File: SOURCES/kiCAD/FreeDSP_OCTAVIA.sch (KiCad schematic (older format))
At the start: 147 parts, among them IC1 TPS5430DDA, J13 Conn_01x05, J2 DC12V-IN, J4 Header_01x06, J8 Header_01x04, P1 Conn_02x20_Odd_Even, Q1 AO3401A, Q14 2N7002, Q2 MMBT5401, Q3 2N7002, Q4 MMBT5401, Q5 AO3401A, Q6 2N7002, Q7 AO3401A, Q8 2N7002, Q9 2N7002, SW1 SW_Push, SW2 SW_SPDT, SW3 SW_SPDT, U1 GP1UXC41QS, U3 AMS1117-5.0, U5 TPS5430DDA, U6 LMC555CMX, U7 AMS1117-3.3, U8 LM2611AMFX

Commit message: Updated version0.2
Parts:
- A1, P1: JLPCB# NOP -> HAND
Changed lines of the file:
@@
 F 2 "Connector_PinSocket_2.54mm:PinSocket_2x20_P2.54mm_Vertical" H 900 6900 50  0001 C CNN
 F 3 "" H 900 6900 50  0001 C CNN
-F 4 "NOP" H 5750 7850 50  0001 C CNN "JLPCB#"
+F 4 "HAND" H 5750 7850 50  0001 C CNN "JLPCB#"
 	1    5750 7850
 	1    0    0    -1
@@
 F 2 "MyLibrary:Combo384" H 8975 8075 50  0001 C CNN
 F 3 "" H 8975 8075 50  0001 C CNN
-F 4 "NOP" H 9175 8125 50  0001 C CNN "JLPCB#"
+F 4 "HAND" H 9175 8125 50  0001 C CNN "JLPCB#"
 	1    9175 8125
 	1    0    0    -1

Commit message: Version0.2 Board. Reviced PCB design.
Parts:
- added D22, D23: 1N4148W, Diode_SMD:D_SOD-123, symbol MW-ADAU1466BB-rescue:D-CS5368TDM-rescue-RasPiAudioHat-rescue
- added J7: Header_01x04, Connector_PinHeader_2.54mm:PinHeader_1x04_P2.54mm_Vertical, symbol Connector_Generic:Conn_01x04
- added Q32: 2N7002, Package_TO_SOT_SMD:SOT-23_Handsoldering, symbol Transistor_FET:2N7002
- added R49: 3.3k, Resistor_SMD:R_0603_1608Metric, symbol Device:R
- added R50: 10k, Resistor_SMD:R_0805_2012Metric_Pad1.20x1.40mm_HandSolder, symbol MW-ADAU1466BB-rescue:R-CS5368TDM-rescue-RasPiAudioHat-rescue
- added R51: 100k, Resistor_SMD:R_0805_2012Metric_Pad1.20x1.40mm_HandSolder, symbol MW-ADAU1466BB-rescue:R-CS5368TDM-rescue-RasPiAudioHat-rescue
- added TP1: TestPoint_GNDA, TestPoint:TestPoint_THTPad_2.0x2.0mm_Drill1.0mm, symbol Connector:TestPoint_Alt
- added TP2: TestPoint_GND, TestPoint:TestPoint_THTPad_2.0x2.0mm_Drill1.0mm, symbol Connector:TestPoint_Alt
- C12: Description (none) -> for the Power-OFF muting power keep
- C13: footprint Capacitor_THT:CP_Radial_D5.0mm_P2.00mm -> Capacitor_THT:CP_Radial_D10.0mm_P2.50mm_P5.00mm; Description (none) -> for Analog +5V decoupling, Solid-Cap recommended
- C15: Description (none) -> for Negative SMPS Power Integration
- C22: Description (none) -> for the Raspberry-pi Shutdown-Time constant
- C43: Description (none) -> for Raspberry-pi SMPS Power Integration
- C8: Description (none) -> for the Power-ON delay timing
- D19: Description (none) -> Just for check the PC status
- D3: Description (none) -> Remove this if you use extension header
- J13: Description (none) -> for the Optional Source Position LED Indicator
- J2: Description (none) -> for 2.1mm wall Power Supply (DC6.5V to 12V)
- J4: Description (none) -> Optional Serial Cable Header for Raspberry-pi
- J8: Description (none) -> Optional I2C OLED Display Connection for Raspberry-pi
- JP3: Description (none) -> Short this if you use sotware DSP-RESET control
- P1: Description (none) -> for Rapberry-pi
- R100, R101, R102, R103: value 330R -> 1k; JLPCB# C17630 -> C17513
- R33, R7: value 1k -> 3.3k; JLPCB# C17513 -> C22978
- SW1: footprint OPL_Switch:SW2-5.0-6.0X3.0X4.3MM -> Button_Switch_THT:SW_Tactile_SPST_Angled_PTS645Vx83-2LFS
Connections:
- net +3.3VP: now also J8.2 (Pin_2); no longer J8.4 (Pin_4)
- net +3V3: now also J13.1 (Pin_1), R108.1, R49.2
- net +5V: no longer J13.1 (Pin_1)
- net AUX5: no longer Q14.3 (D)
- net GND: now also J7.4 (Pin_4), Q32.2 (S), R51.2, TP2.1; no longer R108.1
- net GNDA: now also TP1.1
- net MUTE: now also D22.2 (A); no longer Q9.1 (G)
- net RP_SDA: now also J8.4 (Pin_4); no longer J8.2 (Pin_2)
- net at D3.1 (A), R6.2: now also J7.2 (Pin_2)
- net at D3.3 (GK), Q8.3 (D): now also J7.3 (Pin_3)
- net ~SEL_USB: now reaches J13.2 (Pin_2), R100.2
- net ~SEL_USB: now also R108.2, Q32.1 (G)
- net at A1.11 (~MUTE): now also Q14.1 (G); no longer D13.2 (A)
- net at D3.4 (RK), Q3.3 (D): now also J7.1 (Pin_1)
- net USB_MUTE: no longer names the net of D12.1 (K), D13.1 (K)
- net USB_MUTE: now also R50.1; no longer Q14.1 (G), R108.2
- new net: D22.1 (K), D23.1 (K), Q9.1 (G), R51.1
- new net: D13.2 (A), Q14.3 (D), R49.1
- new net: D23.2 (A), Q32.3 (D), R50.2
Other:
- note added: "1.6V min."
- note added: "ANODE\nRaspberry-Pi\nUSB\nS/PDIF\nANALOG"
- note added: "BLUE\nGREEN\nANODE\nRED"
- note added: "SDA\nSCL\nVCC\nGND"
- note added: "SOURCE MIN MAX\n\n4:Analog 12 - 15\n3:S/PDIF 9 - 11 \n2:USB 6 - 8\n1:RAS-Pi 3 - 5\n0:MUTE 0 - 2"
- note removed: "1.09V/4.8V"
- note removed: "ANODE\nANALOG\nS/PDIF\nUSB\nRaspberry-Pi"
- note removed: "SOURCE MIN MAX\n\nRAS-Pi 12 - 15\nAmanero 9 - 11 \nS/PDIF 6 - 8\nAnalog 3 - 5\nMUTE 0 - 2"
- moved on the sheet: D12, D13, D19, D3, J13, J8, Q14, Q9, R100, R101, R102, R103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

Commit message: Fixed wrong L/R Connection of RCA Jack
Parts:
- A1: symbol MW-ADAU1466BB-rescue:Combo384-Combo384 -> Combo384:Combo384
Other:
- note added: "(ADC/DAC/Line-Driver Power)"
- note added: "DC9V WALL\nADAPTOR"
- note added: "Muting = +12V\nUnMuting = -4.5V"
- note added: "Power-ON Delay \nTiming CR (5 Sec)"
- note removed: "(ADC/DAC Power)"
- note removed: "DC12V WALL\nADOPTOR"
- note removed: "Power-ON Delay \nTiming CR (.1 Sec)"
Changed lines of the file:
@@
 Sheet 1 3
 Title "FreeDSP OVTAVIA Main Board"
-Date "2023-05-13"
+Date "2023-05-21"
 Rev "0.25"
 Comp ""
@@
 Power-OFF Delay \nTiming CR (40 Sec)
 Text Notes 4650 6100 0    50   ~ 0
-Power-ON Delay \nTiming CR (.1 Sec)
+Power-ON Delay \nTiming CR (5 Sec)
 Wire Notes Line
 	5775 5475 5300 5975
@@
 (DSP Power)
 Text Notes 11800 3225 0    50   ~ 0
-(ADC/DAC Power)
+(ADC/DAC/Line-Driver Power)
 $Comp
 L Device:D_ALT D?
@@
 Connection ~ 5750 4175
 Text Notes 11800 3975 0    50   ~ 0
-(ADC/DAC Power)
+(ADC/DAC/Line-Driver Power)
 $Comp
 L Device:C_Small C?
@@
 Connection ~ 3275 1250
 Text Notes 900  1525 0    79   ~ 16
-DC12V WALL\nADOPTOR
+DC9V WALL\nADAPTOR
 Wire Wire Line
 	3275 1150 3275 1250
@@
 $EndComp
 $Comp
-L MW-ADAU1466BB-rescue:Combo384-Combo384 A1
+L Combo384:Combo384 A1
 U 1 1 6517C675
 P 9175 8125
@@
 Text Notes 1850 7400 0    63   ~ 0
 SDA\nSCL\nVCC\nGND
+Text Notes 7100 2350 0    50   ~ 0
+Muting   = +12V\nUnMuting = -4.5V
 $EndSCHEMATC

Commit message: New Output Driver with Enhanced 4 Layer PCB
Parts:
- added C164: 220uF/6.3V, Capacitor_THT:CP_Radial_D10.0mm_P2.50mm_P5.00mm, symbol Device:CP1_Small
- added R54: 100k, Resistor_SMD:R_0805_2012Metric_Pad1.20x1.40mm_HandSolder, symbol MW-ADAU1466BB-rescue:R-CS5368TDM-rescue-RasPiAudioHat-rescue
- J2: value DC12V-IN -> DC7.5V-9V IN
- R33, R7: JLPCB# C22978 -> C26010
- R71: value 330R -> 3.3k; JLPCB# C17630 -> C26010
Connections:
- net +12V: no longer C37.1, C38.1, L4.2, U8.5 (VIN)
- net +3V3: now also R54.1; no longer Q6.1 (G), R35.1, U8.4 (~SHDN)
- net +5VA: now also U8.4 (~SHDN)
- net -5VA: now also C164.2
- net GNDA: now also C164.1
- net ALWAYS_ON: now reaches C14.1, C18.2, C20.1, C21.1, C5.1, C6.1, C9.2, D10.2 (A), D8.1 (K), IC1.7 (VIN), Q1.2 (S), Q5.2 (S), Q7.3, R15.1, R21.1, R36.1, R5.1, SW2.1 (A), U5.7 (VIN), U6.4 (R), U6.8 (VCC)
- net ALWAYS_ON: now also C37.1, C38.1, L4.2, U8.5 (VIN)
- new net: Q6.1 (G), R35.1, R54.2
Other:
- note added: "Muting = +7.5V\nUnMuting = -4.5V"
- note removed: "Muting = +12V\nUnMuting = -4.5V"
- moved on the sheet: C11, C13, C14, C40, C42, C44, C7, FB2, Q5, Q6, R35, R36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

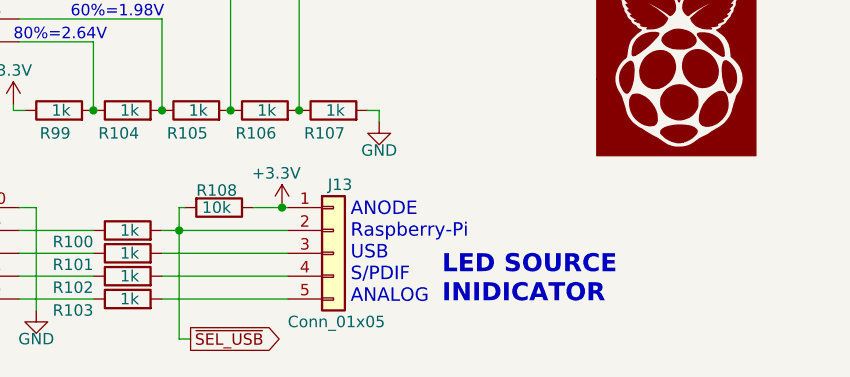
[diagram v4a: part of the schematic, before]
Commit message: Fixed USB Position of Source Selector Switch
Version 0.30 (CCW) USB - RPi - DIG -ANA (CW)
Version 0.31 (CCW) RPi - USB - DIG -ANA (CW)
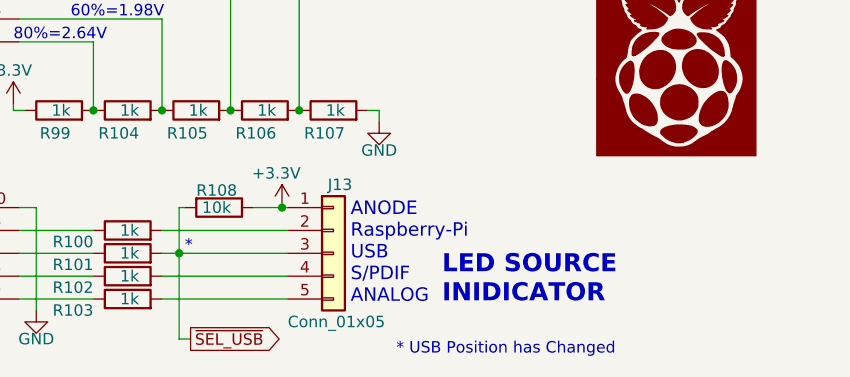
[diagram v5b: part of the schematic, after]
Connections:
- net ~SEL_USB: now also J13.3 (Pin_3), R101.2; no longer J13.2 (Pin_2), R100.2
- new net: J13.2 (Pin_2), R100.2
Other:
- note added: "*"
- note added: "* USB Position has Changed"
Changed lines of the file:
@@
 Sheet 1 3
 Title "FreeDSP OVTAVIA Main Board"
-Date "2023-07-22"
-Rev "0.3"
+Date "2023-07-25"
+Rev "0.31"
 Comp ""
 Comment1 ""
@@
 	4200 10500 4175 10500
 Wire Wire Line
-	4200 10600 3725 10600
-Wire Wire Line
-	3650 10700 4200 10700
+	3650 10700 3725 10700
 Wire Wire Line
 	4200 10800 3650 10800
@@
 Wire Wire Line
 	3750 10500 3725 10500
-Wire Wire Line
-	3725 10500 3725 10600
-Connection ~ 3725 10600
-Wire Wire Line
-	3725 10600 3650 10600
 Text GLabel 3775 11075 2    50   Output ~ 0
 ~SEL_USB
 Wire Wire Line
 	3725 11075 3775 11075
-Wire Wire Line
-	3725 10600 3725 11075
 Text GLabel 9975 9375 0    50   Input ~ 0
 ~SEL_USB
@@
 	15625 2475 15325 2475
 Connection ~ 15325 2475
+Wire Wire Line
+	3650 10600 4200 10600
+Wire Wire Line
+	3725 10500 3725 10700
+Connection ~ 3725 10700
+Wire Wire Line
+	3725 10700 4200 10700
+Wire Wire Line
+	3725 11075 3725 10700
+Text Notes 4675 11150 0    50   ~ 0
+* USB Position has Changed
+Text Notes 3750 10700 0    50   ~ 0
+*
 $EndSCHEMATC

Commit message: Voltage Regulator Changed to LM317
PCB layout is also updated in some of the places.
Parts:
- added R56: 100R, Resistor_SMD:R_0603_1608Metric, symbol Device:R
- added R57: 120R, Resistor_SMD:R_0603_1608Metric, symbol Device:R
- added R58: 330R, Resistor_SMD:R_0603_1608Metric, symbol Device:R
- added R59: 200R, Resistor_SMD:R_0603_1608Metric, symbol Device:R
- added R60: 10R, Resistor_SMD:R_0603_1608Metric, symbol Device:R
- A1: Description (none) -> Amanero or Compatible USB to I2S I/F Board Slot
- D19: Description Just for check the PC status -> Just for check the PC VBUS status
- D3: Description Remove this if you use extension header -> Remove this if you use the Power Status LED extension header
- FL1: Description (none) -> Common mode choke for mains
- IC1, U5: Description (none) -> SMPS for digital part
- J2: Description for 2.1mm wall Power Supply (DC6.5V to 12V) -> for 2.1mm wall Power Supply (DC6.5V to 9V)
- J4: Description Optional Serial Cable Header for Raspberry-pi -> Optional TTL-232R-3V3 Serial Cable Header for Raspberry-pi
- L2, L3, L4, L5: Description (none) -> Metal-Alloy Power Inductor
- MH1: Description (none) -> Mount-hole for Chassis GND
- SW1: Description (none) -> RPI Shutdown/Reboot switch
- SW2: Description (none) -> Mains Power Switch C&K 200MSP1T2B2M7RE, T105MH9AVBE
- SW3: Description (none) -> RPI Power Sub-Switch C&K 200MSP1T2B2M7RE, T105MH9AVBE
- TP1: Description (none) -> TP for Analog Measurement
- TP2: Description (none) -> for Chassis GND Connection
- U1: Description SENSOR REMOTE REC 38.0KHZ 45M -> Optional: Vishay TSOP38238 IR REMOTE SENSOR REC 38.0KHZ 45M
- U3: value AMS1117-5.0 -> LM317AG-TN3-R; footprint Package_TO_SOT_SMD:SOT-223-3_TabPin2 -> Package_TO_SOT_SMD:TO-252-2; symbol Regulator_Linear:AZ1117-ADJ -> Regulator_Linear:LM317_TO-252; Description (none) -> Voltage Regurator for Analog; JLPCB# C6187 -> C75510
- U6: Description (none) -> Timing Controller for RPI PSU
- U7: value AMS1117-3.3 -> LM317AG-TN3-R; footprint Package_TO_SOT_SMD:SOT-223-3_TabPin2 -> Package_TO_SOT_SMD:TO-252-2; symbol Regulator_Linear:AZ1117-ADJ -> Regulator_Linear:LM317_TO-252; Description (none) -> Voltage Regurator for Analog; JLPCB# C6186 -> C75510
- U8: Description (none) -> Negativer 3MHz SMPS
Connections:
- net +3.3VA: now also R57.1
- net +5VA: now also R60.1
- net GND: no longer C140.1
- net GNDA: now also C140.1, R58.1, R59.1; no longer U3.1 (ADJ), U7.1 (ADJ)
- new net: R56.2, R58.2, U3.1 (ADJ)
- new net: R57.2, R59.2, U7.1 (ADJ)
- new net: R56.1, R60.2
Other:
- note added: "1.4MHz Invert SMPS"
- note added: "2.08V"
- note added: "3.75V"
- note added: "C&K 200MSP1T2B2M7RE, T105MH9AVBE"
- note added: "C&K PTS645VL39-2 LFS"
- note added: "RAS-Pi\nSHUT/REBOOT\nSWITCH"
- note removed: "RAS-Pi\nRES/SHUT\nSWITCH"
- moved on the sheet: C40, C42, C44, U7

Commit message: Released for everyone, ready to build.
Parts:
- removed Q14: 2N7002, Package_TO_SOT_SMD:SOT-23_Handsoldering, symbol Transistor_FET:2N7002
- added R61: 0R, Resistor_SMD:R_0603_1608Metric, symbol Device:R
- A1: value Combo384 -> Combo384-Combo384
- C22: Description for the Raspberry-pi Shutdown-Time constant -> Time-Constant Cap for RPI delay-Shutdown
- C23: Description (none) -> Time-Constant Cap for RPI delay-ON
- D1, D11, D12, D13, D2, D22, D23, D4, D5, D6, D7, D8: Description (none) -> Si Switching Diode
- D10, D9: Description (none) -> SBD for charging C32
- D14, D16: Description (none) -> SBD 40V 550mV@5A
- FB13: Description FERRITE BEAD 600 OHM 0603 1LN -> Bead for Analog -VEE rail
- MH2, MH3, MH4, MH5, MH6, MH7: Description (none) -> Mount hole
- MK1, MK2: Description (none) -> Mount hole for Rspberry-pi
- P1: Description for Rapberry-pi -> for Rapberry-pi Slot
- Q2, Q4: Description (none) -> PNP Transistor for anti-pop muting
- Q3, Q32, Q6, Q8, Q9: Description (none) -> N-CHANNEL ENHANCEMENT MODE MOSFET
- R10, R9: Description (none) -> Selectable Exclusive Mount Jumper R
- R40: Description (none) -> Selectable Exclusive Mount Jumper for RESET by RPI feature
- R49: value 3.3k -> 10k; JLPCB# C22978 -> C25804
- R57: value 120R -> 180R
- R59: value 200R -> 270R
- TP1: Description TP for Analog Measurement -> TP for Analog Measurement and Chassis GND Connection
- TP2: Description for Chassis GND Connection -> TP for Digital Measurement
- U1: Description Optional: Vishay TSOP38238 IR REMOTE SENSOR REC 38.0KHZ 45M -> Optional: IR REMOTE SENSOR Vishay TSOP38238 38.0KHZ 45M
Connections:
- net +3V3: no longer R49.2
- net GND: now also R49.1, R61.1
- net GNDA: now also R61.2
- net at A1.11 (MUTE): now also D13.2 (A), R49.2
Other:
- note added: "2.05V"
- note removed: "2.08V"
- moved on the sheet: R49
